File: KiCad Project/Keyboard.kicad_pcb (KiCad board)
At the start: 2 copper layers, 50.8 x 59.5 mm, 36 parts, among them SW1 SW_Push, SW2 SW_Push, SW3 SW_Push, U1 ATmega32U2-AU, Y1 Crystal_GND24_Small

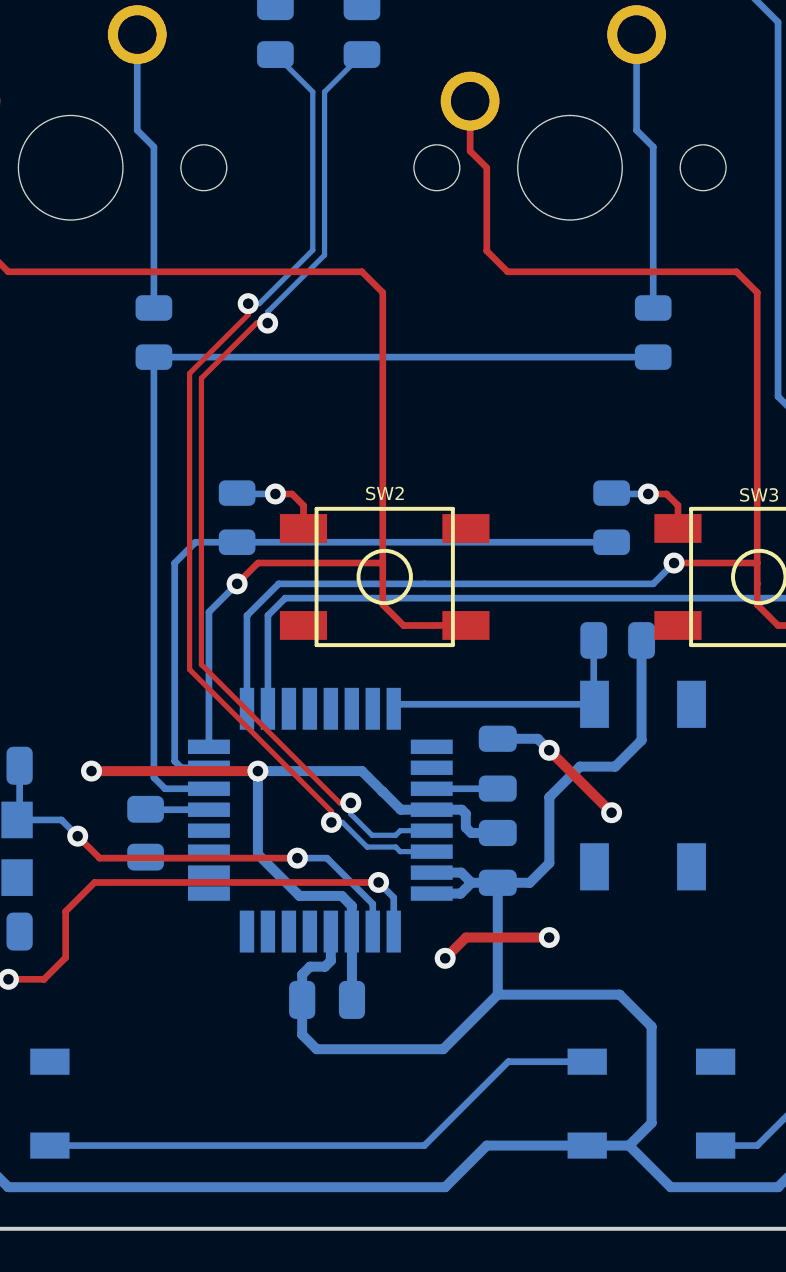
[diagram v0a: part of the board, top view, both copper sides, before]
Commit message: Gerber with ground lines added
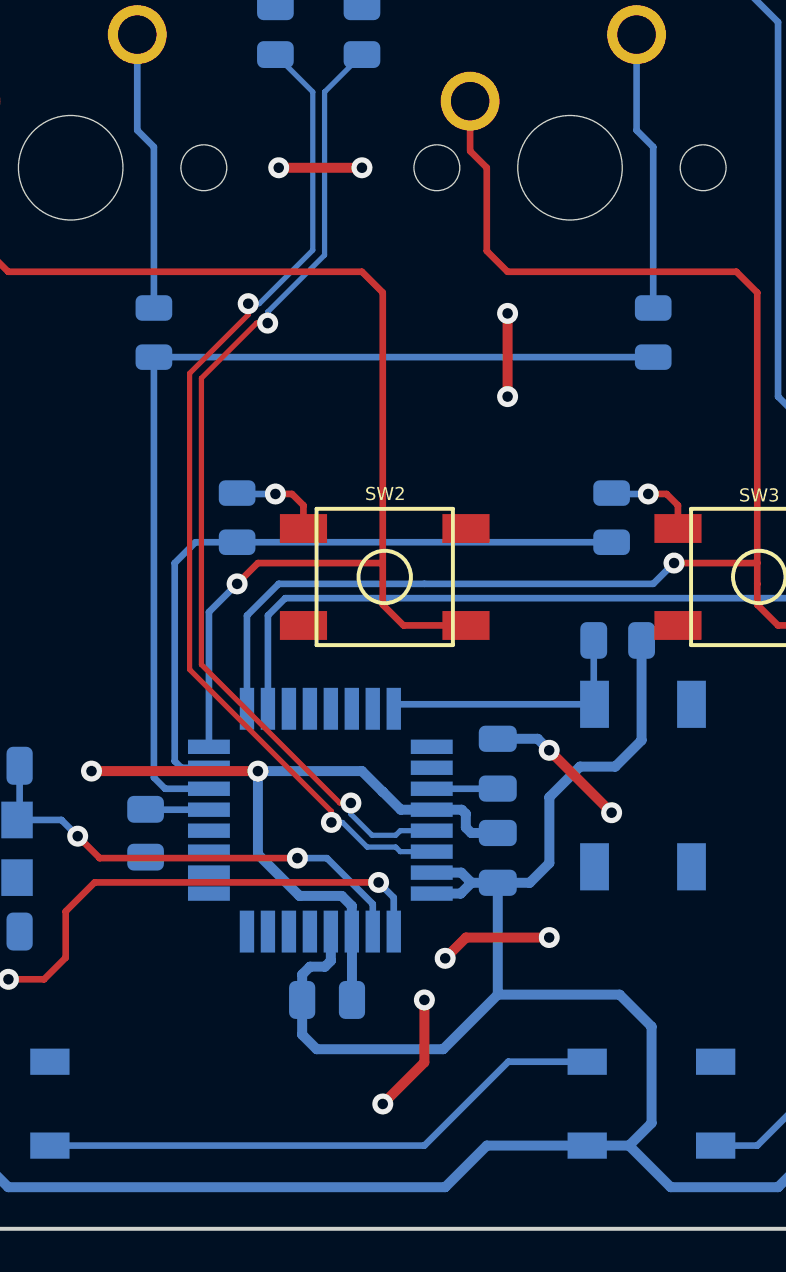
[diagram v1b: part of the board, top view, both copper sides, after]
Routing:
- net GND: track 41.3 -> 52.3 mm, vias 6 -> 12
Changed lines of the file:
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@@
     (thickness 1.6)
     (drawings 8)
-    (tracks 306)
+    (tracks 316)
     (zones 0)
     (modules 36)
@@
   (segment (start 93.7125 43.7015) (end 93.7125 44.2075) (width 0.381) (layer B.Cu) (net 2))
   (segment (start 94.1215 43.2925) (end 93.7125 43.7015) (width 0.381) (layer B.Cu) (net 2))
+  (via (at 92.86875 92.86875) (size 0.8) (drill 0.4) (layers F.Cu B.Cu) (net 2))
+  (via (at 94.45625 88.9) (size 0.8) (drill 0.4) (layers F.Cu B.Cu) (net 2))
+  (segment (start 92.86875 92.86875) (end 94.45625 91.28125) (width 0.381) (layer F.Cu) (net 2))
+  (segment (start 94.45625 91.28125) (end 94.45625 88.9) (width 0.381) (layer F.Cu) (net 2))
+  (via (at 97.63125 62.70625) (size 0.8) (drill 0.4) (layers F.Cu B.Cu) (net 2))
+  (via (at 97.63125 65.88125) (size 0.8) (drill 0.4) (layers F.Cu B.Cu) (net 2))
+  (segment (start 97.63125 62.70625) (end 97.63125 65.88125) (width 0.381) (layer F.Cu) (net 2))
+  (via (at 92.075 57.15) (size 0.8) (drill 0.4) (layers F.Cu B.Cu) (net 2))
+  (via (at 88.9 57.15) (size 0.8) (drill 0.4) (layers F.Cu B.Cu) (net 2))
+  (segment (start 92.075 57.15) (end 88.9 57.15) (width 0.381) (layer F.Cu) (net 2))
   (segment (start 77.1144 84.33435) (end 77.216 84.23275) (width 0.254) (layer B.Cu) (net 3))
   (segment (start 77.1144 86.29015) (end 77.1144 84.33435) (width 0.254) (layer B.Cu) (net 3))
